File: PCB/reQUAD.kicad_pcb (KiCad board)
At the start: 2 copper layers, 49.5 x 16.5 mm, 8 parts, among them J1 Model_100_System_BUS, U1 74LVC2G79, U2 74AC02, U4 74AC573, U5 628128

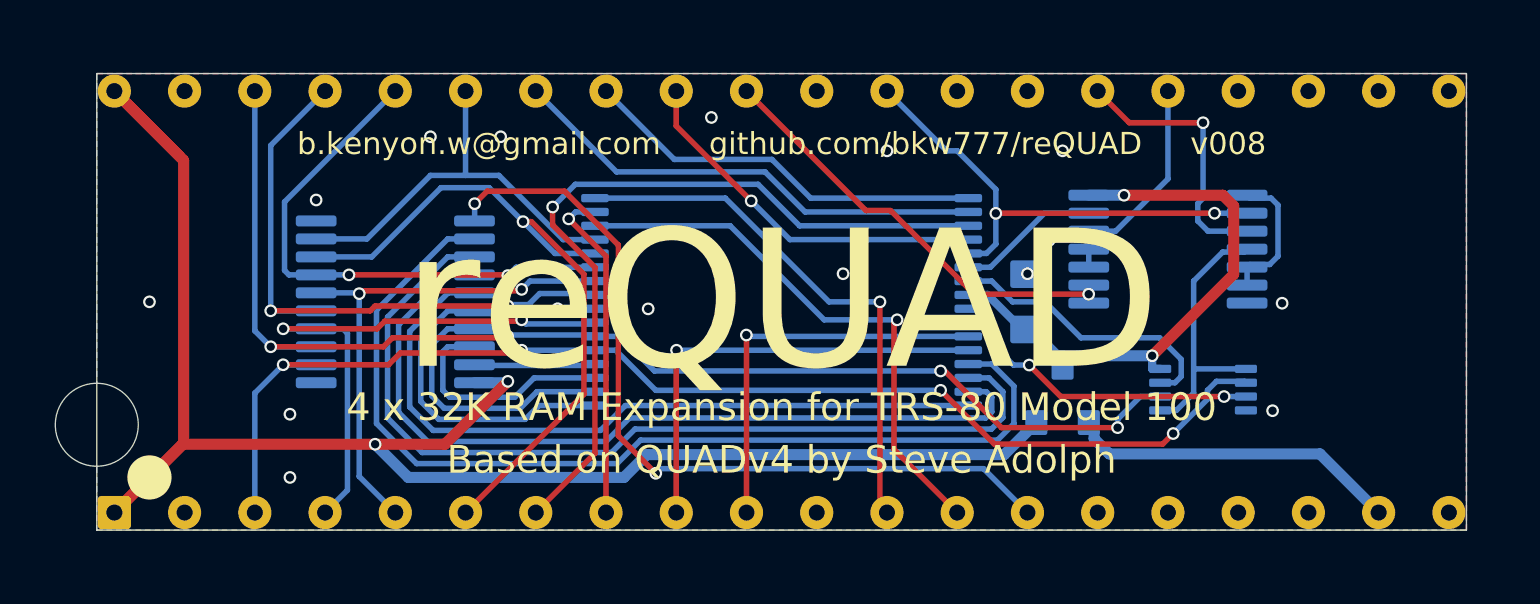
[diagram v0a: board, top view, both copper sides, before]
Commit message: Try Steve's new idea: Pull (A)* low instead of pulling RAMRST high
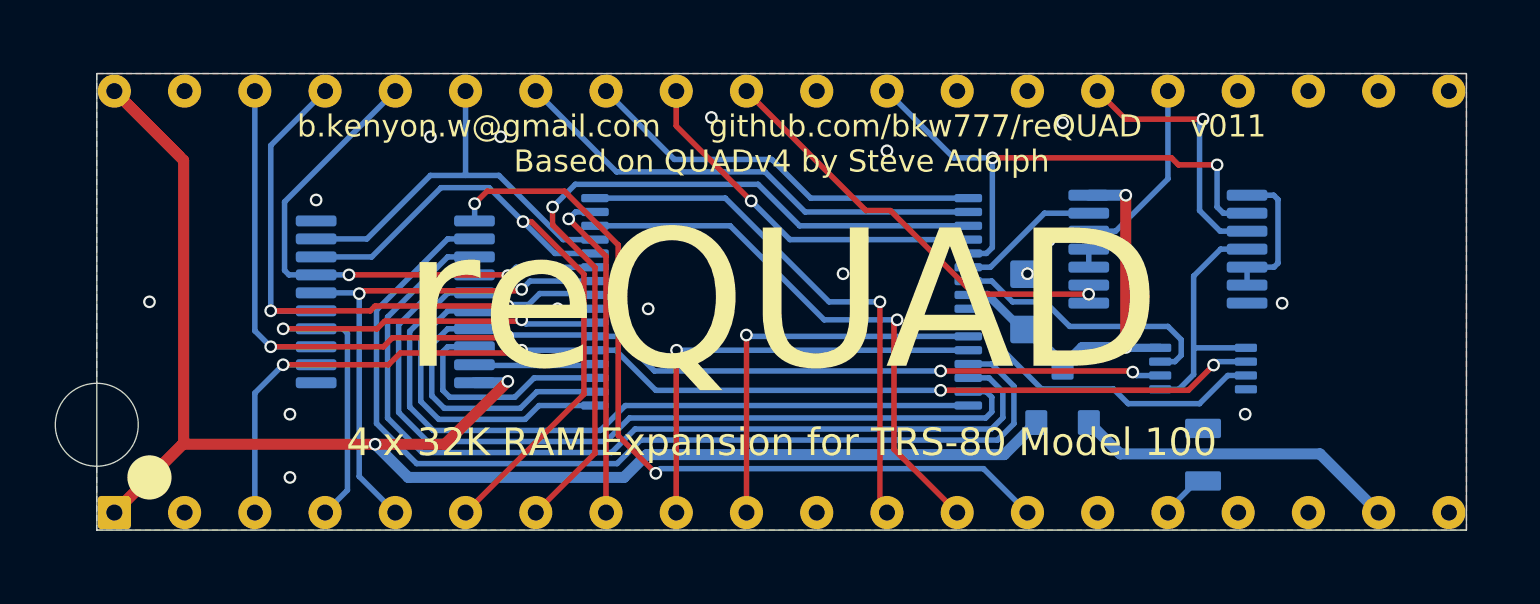
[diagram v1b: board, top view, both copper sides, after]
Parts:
- added R1: 0, 000_LOCAL:R_0805, B.Cu at (165.2, 105.5)
- moved U1 0.76 mm to (165.2, 102.4)
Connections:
- net /ALE renamed /ALE*
- net /IO~{M} renamed /IO~{M}*
- net /RESET renamed /RESET*
- net /~{RD} renamed /~{RD}*
- net /~{WR} renamed /~{WR}*
- J1 pad 16: unconnected-(J1-Pad16) -> /(A)*
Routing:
- net VMEM: track 20.8 -> 15.2 mm
- net /~{WR}*: track 17.6 -> 19.9 mm
- net /(A)*: track 0.00 -> 1.80 mm
- net /AD0: track 44.5 -> 43.0 mm
- net /AD1: track 45.5 -> 44.1 mm
- net /FLOP_CLK: track 9.81 -> 9.18 mm
- net /B1: track 11.5 -> 11.9 mm, vias 2 -> 0
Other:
- board text added: "b.kenyon.w@gmail.com github.com/bkw777/reQUAD v011"
- board text added: "this side down / legs this side"
- board text removed: "b.kenyon.w@gmail.com github.com/bkw777/reQUAD v008"
- board text removed: "this side down - legs this side"

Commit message: pcb routing vcc vmem A0-A3
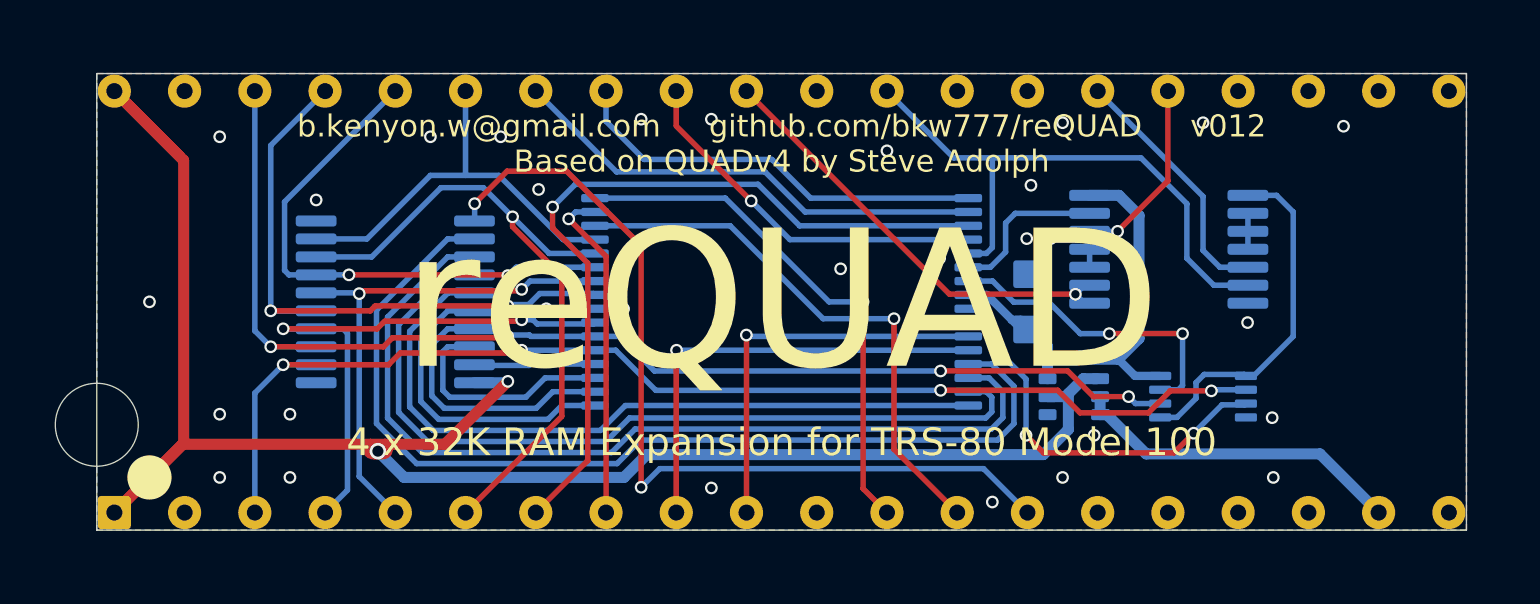
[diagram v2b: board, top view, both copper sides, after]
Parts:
- removed R1: 0, 000_LOCAL:R_0805
- D1: value BAV70 -> BAV70S; footprint 000_LOCAL:SOT-23 -> 000_LOCAL:SOT-363_symmetric
- moved U1 1.02 mm to (165.2, 103.4)
- moved D1 0.41 mm to (160.6, 103.4), turned to 180 degrees
- moved C1 0.11 mm to (159.0, 100.0)
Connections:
- D1 pad 1: /RAMRST -> VCC
- D1 pad 2: VCC -> /RAMRST
- D1 pad 3: VMEM -> /RAMRST
- U2 pad 1: Net-(U2-Pad1) -> /FLOP_CLK
- U2 pad 2: /~{WR}* -> Net-(U2-Pad2)
- U2 pad 3: /~{Y0} -> Net-(U2-Pad2)
- U2 pad 4: /FLOP_CLK -> Net-(U2-Pad2)
- U2 pad 5: Net-(U2-Pad1) -> /~{Y0}
- U2 pad 6: Net-(U2-Pad1) -> /~{WR}*
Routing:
- net Net-(U2-Pad1): track 5.31 -> 0.00 mm
- net VCC: track 63.3 -> 68.1 mm
- net /FLOP_CLK: track 9.18 -> 12.9 mm
- net /B1: track 11.9 -> 14.3 mm, vias 0 -> 2
- net VMEM: track 15.2 -> 17.5 mm, vias 2 -> 0
- net /ALE*: track 29.8 -> 31.9 mm
- net /(A)*: track 1.80 -> 0.00 mm
- net /~{WR}*: track 19.9 -> 21.3 mm, vias 2 -> 0
- net Net-(U2-Pad2): track 0.00 -> 1.30 mm
- net /B0: track 10.00 -> 11.3 mm, vias 0 -> 2
- net /U5_CE2: track 5.17 -> 5.81 mm
- net /A11: track 14.7 -> 15.3 mm
- net /AD6: track 25.5 -> 25.0 mm
- net /~{Y0}: track 9.61 -> 9.21 mm, vias 1 -> 0
- net /RESET*: track 6.82 -> 6.84 mm, vias 0 -> 1
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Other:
- board text added: "b.kenyon.w@gmail.com github.com/bkw777/reQUAD v012"
- board text removed: "b.kenyon.w@gmail.com github.com/bkw777/reQUAD v011"

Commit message: vcc routing
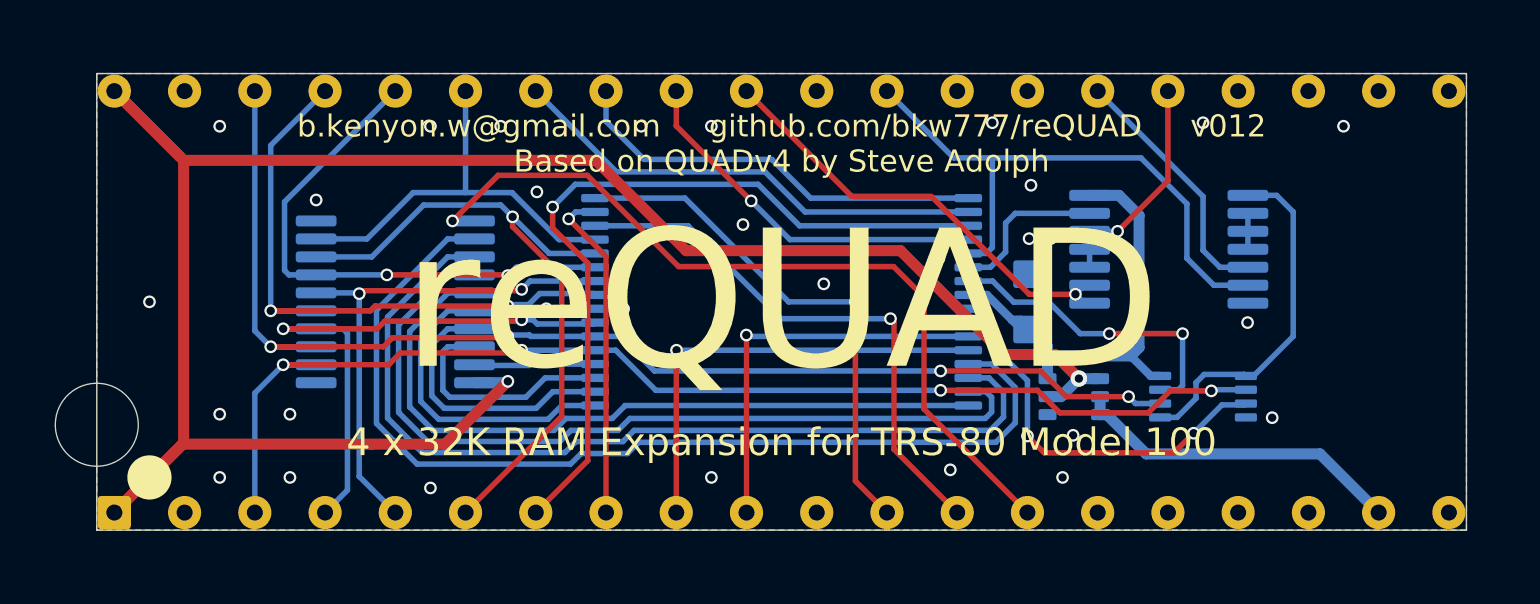
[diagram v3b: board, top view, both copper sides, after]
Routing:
- net VCC: track 68.1 -> 75.8 mm
- net /ALE*: track 31.9 -> 29.7 mm, vias 2 -> 1
- net /AD6: track 25.0 -> 24.5 mm
- net GND: vias 31 -> 30

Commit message: renders and minor pcb layout adjustments
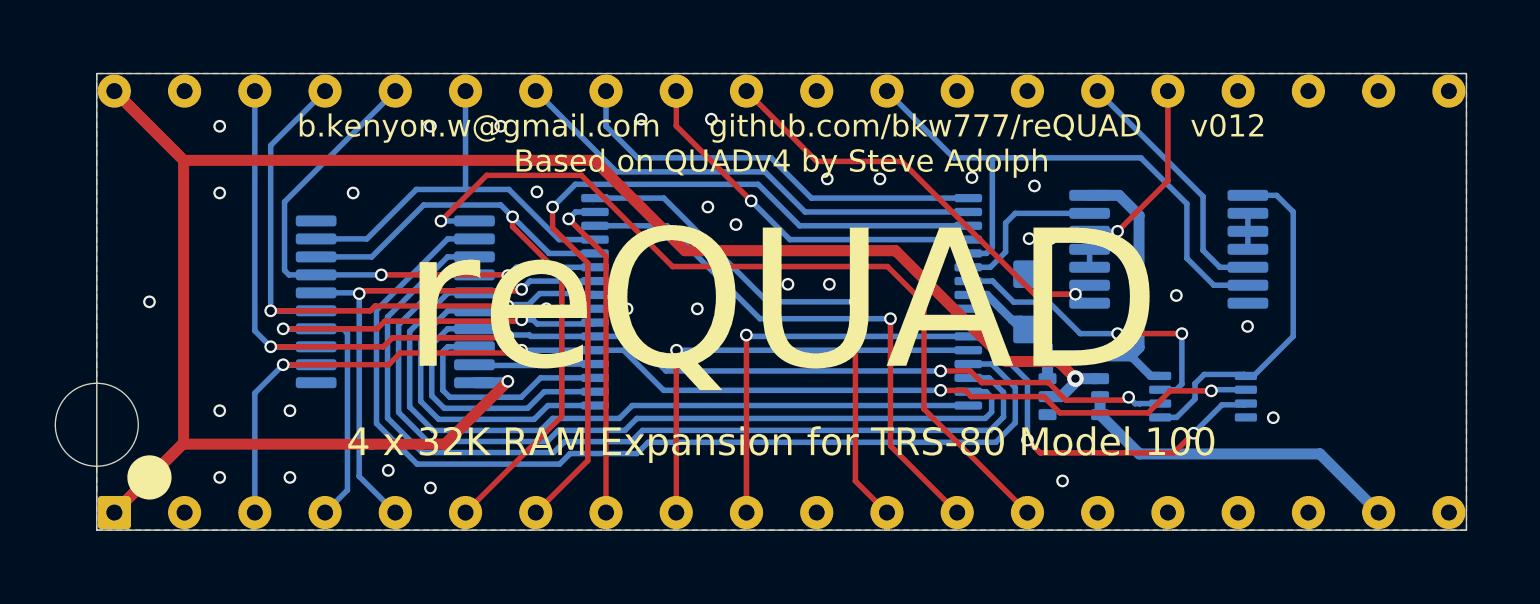
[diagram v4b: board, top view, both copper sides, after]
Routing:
- net /ALE*: track 29.7 -> 30.4 mm
- net GND: vias 30 -> 33

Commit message: dip pins footprint & board outline
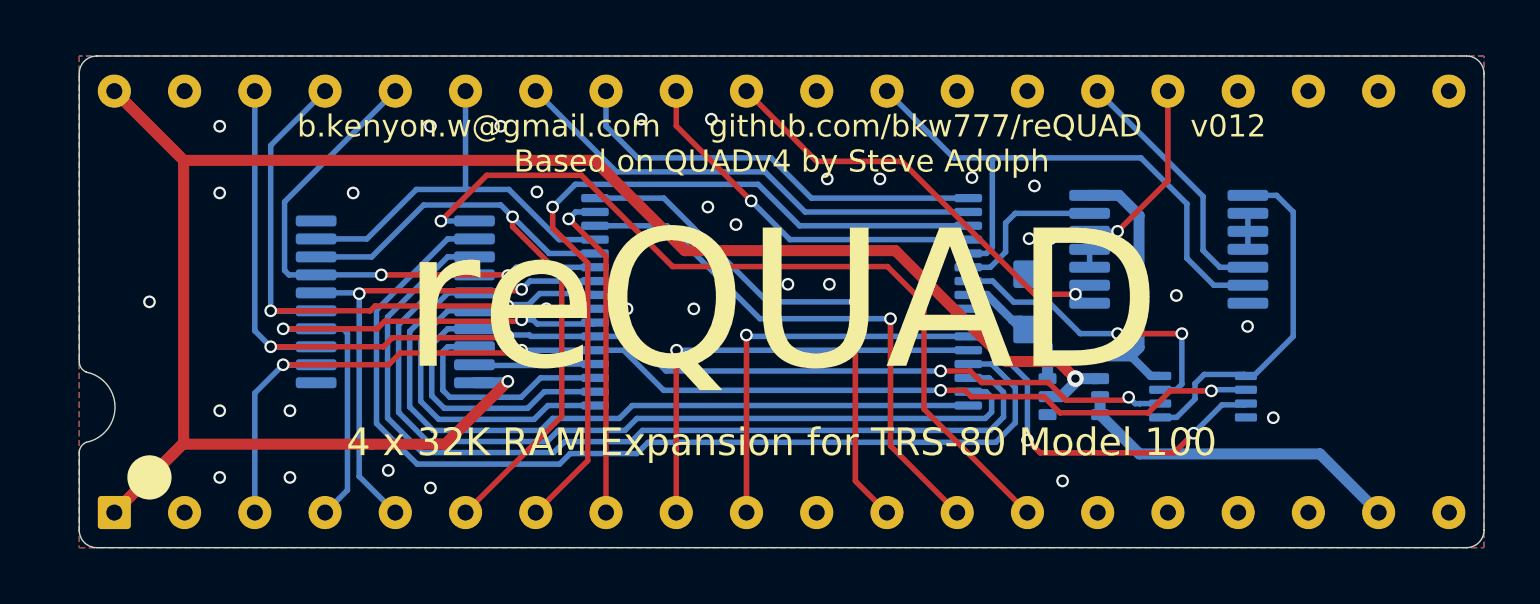
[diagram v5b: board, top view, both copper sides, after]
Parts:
- removed REF**: NPTH_3mm, 000_LOCAL:NPTH_3mm
- J1: moved to B.Cu
- moved J1 25.3 mm to (150.0, 100.0), turned to 0 degrees
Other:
- board size 49.5 x 16.5 mm -> 50.8 x 17.8 mm

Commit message: outline, fiducials
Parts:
- added REF**: Fiducial_0.5_1.0, 000_LOCAL:Fiducial_0.5_1.0, B.Cu at (125.9, 94.9)
- added REF**: Fiducial_0.5_1.0, 000_LOCAL:Fiducial_0.5_1.0, B.Cu at (174.0, 94.9)
- added REF**: Fiducial_0.5_1.0, 000_LOCAL:Fiducial_0.5_1.0, B.Cu at (174.0, 105.1)
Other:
- outline, holes or cut-outs redrawn
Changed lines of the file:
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@@
   (title_block
     (title "reQUAD")
-    (date "2022-08-29")
+    (date "2022-08-30")
     (rev "012")
     (company "Brian K. White - b.kenyon.w@gmail.com")
@@
     (grid_origin 150 100)
     (pcbplotparams
-      (layerselection 0x00010f0_ffffffff)
+      (layerselection 0x00010fc_ffffffff)
       (disableapertmacros false)
       (usegerberextensions true)
@@
     )
   )
+  (footprint "000_LOCAL:Fiducial_0.5_1.0" (layer "B.Cu")
+    (at 125.87 94.92 180)
+    (descr "Circular Fiducial, 0.5mm bare copper, 1mm soldermask opening (Level C)")
+    (tags "fiducial")
+    (attr smd)
+    (fp_text reference "REF**" (at 0 1.5) (layer "B.SilkS") hide
+      (effects (font (size 1 1) (thickness 0.15)) (justify mirror))
+    )
+    (fp_text value "Fiducial_0.5_1.0" (at 0 -1.5) (layer "B.Fab") hide
+      (effects (font (size 1 1) (thickness 0.15)) (justify mirror))
+    )
+    (fp_text user "${REFERENCE}" (at 0 0) (layer "B.Fab") hide
+      (effects (font (size 0.2 0.2) (thickness 0.04)) (justify mirror))
+    )
+    (fp_circle (center 0 0) (end 0.75 0) (layer "B.CrtYd") (width 0.05) (fill none))
+    (fp_circle (center 0 0) (end 0.5 0) (layer "B.Fab") (width 0.1) (fill none))
+    (pad "" smd circle (at 0 0 180) (size 0.5 0.5) (layers "B.Cu" "B.Mask")
+      (solder_mask_margin 0.25) (clearance 0.25))
+  )
   (footprint "000_LOCAL:SOT-363_symmetric" (layer "B.Cu")
     (at 160.5664 103.429 180)
@@
     )
   )
+  (footprint "000_LOCAL:Fiducial_0.5_1.0" (layer "B.Cu")
+    (at 174.003 94.92 180)
+    (descr "Circular Fiducial, 0.5mm bare copper, 1mm soldermask opening (Level C)")
+    (tags "fiducial")
+    (attr smd)
+    (fp_text reference "REF**" (at 0 1.5) (layer "B.SilkS") hide
+      (effects (font (size 1 1) (thickness 0.15)) (justify mirror))
+    )
+    (fp_text value "Fiducial_0.5_1.0" (at 0 -1.5) (layer "B.Fab") hide
+      (effects (font (size 1 1) (thickness 0.15)) (justify mirror))
+    )
+    (fp_text user "${REFERENCE}" (at 0 0) (layer "B.Fab") hide
+      (effects (font (size 0.2 0.2) (thickness 0.04)) (justify mirror))
+    )
+    (fp_circle (center 0 0) (end 0.75 0) (layer "B.CrtYd") (width 0.05) (fill none))
+    (fp_circle (center 0 0) (end 0.5 0) (layer "B.Fab") (width 0.1) (fill none))
+    (pad "" smd circle (at 0 0 180) (size 0.5 0.5) (layers "B.Cu" "B.Mask")
+      (solder_mask_margin 0.25) (clearance 0.25))
+  )
+  (footprint "000_LOCAL:Fiducial_0.5_1.0" (layer "B.Cu")
+    (at 174.003 105.08 180)
+    (descr "Circular Fiducial, 0.5mm bare copper, 1mm soldermask opening (Level C)")
+    (tags "fiducial")
+    (attr smd)
+    (fp_text reference "REF**" (at 0 1.5) (layer "B.SilkS") hide
+      (effects (font (size 1 1) (thickness 0.15)) (justify mirror))
+    )
+    (fp_text value "Fiducial_0.5_1.0" (at 0 -1.5) (layer "B.Fab") hide
+      (effects (font (size 1 1) (thickness 0.15)) (justify mirror))
+    )
+    (fp_text user "${REFERENCE}" (at 0 0) (layer "B.Fab") hide
+      (effects (font (size 0.2 0.2) (thickness 0.04)) (justify mirror))
+    )
+    (fp_circle (center 0 0) (end 0.75 0) (layer "B.CrtYd") (width 0.05) (fill none))
+    (fp_circle (center 0 0) (end 0.5 0) (layer "B.Fab") (width 0.1) (fill none))
+    (pad "" smd circle (at 0 0 180) (size 0.5 0.5) (layers "B.Cu" "B.Mask")
+      (solder_mask_margin 0.25) (clearance 0.25))
+  )
   (gr_circle (center 127.14 106.35) (end 126.74 106.35) (layer "F.SilkS") (width 0.8) (fill none))
-  (gr_line (start 174.765 91.11) (end 125.235 91.11) (layer "Edge.Cuts") (width 0.05))
-  (gr_line (start 124.6 108.255) (end 124.6 105.461) (layer "Edge.Cuts") (width 0.05))
-  (gr_line (start 124.6 102.159) (end 124.6 91.745) (layer "Edge.Cuts") (width 0.05))
-  (gr_arc (start 175.4 108.255) (mid 175.214013 108.704013) (end 174.765 108.89) (layer "Edge.Cuts") (width 0.05))
-  (gr_arc (start 174.765 91.11) (mid 175.214013 91.295987) (end 175.4 91.745) (layer "Edge.Cuts") (width 0.05))
-  (gr_arc (start 124.6 91.745) (mid 124.785987 91.295987) (end 125.235 91.11) (layer "Edge.Cuts") (width 0.05))
-  (gr_arc (start 124.854 102.54) (mid 124.669321 102.387953) (end 124.6 102.159) (layer "Edge.Cuts") (width 0.05))
-  (gr_arc (start 125.235 108.89) (mid 124.785987 108.704013) (end 124.6 108.255) (layer "Edge.Cuts") (width 0.05))
-  (gr_arc (start 124.854 102.540001) (mid 125.89515 103.81) (end 124.854 105.079999) (layer "Edge.Cuts") (width 0.05))
-  (gr_arc (start 124.6 105.461) (mid 124.669321 105.232047) (end 124.854 105.08) (layer "Edge.Cuts") (width 0.05))
-  (gr_line (start 175.4 108.255) (end 175.4 91.745) (layer "Edge.Cuts") (width 0.05))
-  (gr_line (start 125.235 108.89) (end 174.765 108.89) (layer "Edge.Cuts") (width 0.05))
+  (gr_line (start 174.638 91.11) (end 125.362 91.11) (layer "Edge.Cuts") (width 0.05))
+  (gr_line (start 124.6 108.128) (end 124.6 105.334) (layer "Edge.Cuts") (width 0.05))
+  (gr_line (start 124.6 102.286) (end 124.6 91.872) (layer "Edge.Cuts") (width 0.05))
+  (gr_arc (start 175.4 108.128) (mid 175.176815 108.666815) (end 174.638 108.89) (layer "Edge.Cuts") (width 0.05))
+  (gr_arc (start 124.6 105.334) (mid 124.674395 105.154395) (end 124.854 105.08) (layer "Edge.Cuts") (width 0.05))
+  (gr_arc (start 174.638 91.11) (mid 175.176815 91.333185) (end 175.4 91.872) (layer "Edge.Cuts") (width 0.05))
+  (gr_arc (start 124.854 102.54) (mid 124.674395 102.465605) (end 124.6 102.286) (layer "Edge.Cuts") (width 0.05))
+  (gr_arc (start 124.6 91.872) (mid 124.823185 91.333185) (end 125.362 91.11) (layer "Edge.Cuts") (width 0.05))
+  (gr_arc (start 124.854 102.54) (mid 125.893091 103.81) (end 124.854 105.08) (layer "Edge.Cuts") (width 0.05))
+  (gr_line (start 175.4 108.128) (end 175.4 91.872) (layer "Edge.Cuts") (width 0.05))
+  (gr_line (start 125.362 108.89) (end 174.638 108.89) (layer "Edge.Cuts") (width 0.05))
+  (gr_arc (start 125.362 108.89) (mid 124.823185 108.666815) (end 124.6 108.128) (layer "Edge.Cuts") (width 0.05))
   (gr_text "this side down / legs this side" (at 150 94.92) (layer "B.SilkS")
     (effects (font (size 0.8 0.8) (thickness 0.1)) (justify mirror))
@@
   (segment (start 135.35 100.3) (end 137.925 97.725) (width 0.2) (layer "B.Cu") (net 32))
   (segment (start 128.34 105.15) (end 125.87 107.62) (width 0.4) (layer "F.Cu") (net 33))
+  (segment (start 154.119 98.15) (end 146.372 98.15) (width 0.4) (layer "F.Cu") (net 33))
   (segment (start 135.175 105.15) (end 137.825 105.15) (width 0.4) (layer "F.Cu") (net 33))
+  (segment (start 146.372 98.15) (end 143.107 94.885) (width 0.4) (layer "F.Cu") (net 33))
   (segment (start 128.375 105.115) (end 125.87 107.62) (width 0.4) (layer "F.Cu") (net 33))
-  (segment (start 146.499 98.15) (end 143.234 94.885) (width 0.4) (layer "F.Cu") (net 33))
-  (segment (start 143.234 94.885) (end 128.375 94.885) (width 0.4) (layer "F.Cu") (net 33))
   (segment (start 128.375 94.885) (end 128.375 105.115) (width 0.4) (layer "F.Cu") (net 33))
   (segment (start 128.24 94.75) (end 125.87 92.38) (width 0.4) (layer "F.Cu") (net 33))
   (segment (start 125.87 92.38) (end 128.375 94.885) (width 0.4) (layer "F.Cu") (net 33))
   (segment (start 135.15 105.15) (end 128.34 105.15) (width 0.4) (layer "F.Cu") (net 33))
-  (segment (start 154.119 98.15) (end 146.499 98.15) (width 0.4) (layer "F.Cu") (net 33))
+  (segment (start 158.128 102.159) (end 154.119 98.15) (width 0.4) (layer "F.Cu") (net 33))
   (segment (start 160.625 102.775) (end 160.009 102.159) (width 0.4) (layer "F.Cu") (net 33))
-  (segment (start 158.128 102.159) (end 154.119 98.15) (width 0.4) (layer "F.Cu") (net 33))
+  (segment (start 160.009 102.159) (end 158.128 102.159) (width 0.4) (layer "F.Cu") (net 33))
+  (segment (start 143.107 94.885) (end 128.375 94.885) (width 0.4) (layer "F.Cu") (net 33))
   (segment (start 137.825 105.15) (end 140.1 102.875) (width 0.4) (layer "F.Cu") (net 33))
-  (segment (start 160.009 102.159) (end 158.128 102.159) (width 0.4) (layer "F.Cu") (net 33))
   (via (at 160.625 102.775) (size 0.6) (drill 0.3) (layers "F.Cu" "B.Cu") (net 33))
   (via (at 140.1 102.875) (size 0.46) (drill 0.3) (layers "F.Cu" "B.Cu") (net 33))
